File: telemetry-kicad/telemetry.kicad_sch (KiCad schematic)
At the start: 126 parts, among them J1 2601-1102, J2 RFPC-SMA27-F, J3 TC2030, J4 2601-1102, J5 MOLEX_104031-0811, J6 2601-1102, J7 USB_C_Receptacle_USB2.0_16P, Q1 DMP3099LQ-7, Q2 MMBT3904, SW1 CJS-1200TB1, SW2 CJS-1200TB1, SW3 SW_NRST, SW4 SW_BOOT0, U1 LMR33610ADDAR, U10 LC29HBAMD, U11 USBLC6-2SC6, U12 TXS0108EPW, U2 TPS2121RUXR, U3 ASM330LHHXG1TR, U4 TCAN337, U5 LM2940CT-5.0/LF01, U6 STM32H523RCT7, U7 TCAN337, U8 TLC59108IPWR, U9 TLC59108IPWR, Y1 ABM8AIG-24.000MHz-8-2Z-T

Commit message: ERC errors cleared
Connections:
- no-connect marks 15 -> 30
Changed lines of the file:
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@@
 	)
 	(no_connect
+		(at 100.33 176.53)
+	)
+	(no_connect
+		(at 100.33 179.07)
+	)
+	(no_connect
+		(at 100.33 181.61)
+	)
+	(no_connect
+		(at 39.37 186.69)
+	)
+	(no_connect
+		(at 39.37 189.23)
+	)
+	(no_connect
+		(at 39.37 191.77)
+	)
+	(no_connect
+		(at 39.37 217.17)
+	)
+	(no_connect
+		(at 39.37 219.71)
+	)
+	(no_connect
+		(at 39.37 181.61)
+	)
+	(no_connect
+		(at 353.06 172.72)
+	)
+	(no_connect
+		(at 353.06 175.26)
+	)
+	(no_connect
+		(at 353.06 177.8)
+	)
+	(no_connect
+		(at 410.21 172.72)
+	)
+	(no_connect
+		(at 410.21 175.26)
+	)
+	(no_connect
+		(at 410.21 177.8)
+	)
+	(no_connect
 		(at 171.45 217.17)
 	)
@@
 					(unit 1)
 				)
+			)
+		)
+	)
+	(symbol
+		(lib_id "power:PWR_FLAG")
+		(at 393.7 27.94 0)
+		(unit 1)
+		(body_style 1)
+		(exclude_from_sim no)
+		(in_bom yes)
+		(on_board yes)
+		(in_pos_files yes)
+		(dnp no)
+		(property "Reference" "#FLG01"
+			(at 393.7 29.845000000000002 0)
+			(hide yes)
+			(show_name no)
+			(do_not_autoplace no)
+			(effects
+				(font
+					(size 1.27 1.27)
+				)
+			)
+		)
+		(property "Value" "PWR_FLAG"
+			(at 393.7 31.75 0)
+			(show_name no)
+			(do_not_autoplace no)
+			(effects
+				(font
+					(size 1.27 1.27)
+				)
+			)
+		)
+		(property "Footprint" ""
+			(at 393.7 27.94 0)
+			(hide yes)
+			(show_name no)
+			(do_not_autoplace no)
+			(effects
+				(font
+					(size 1.27 1.27)
+				)
+			)
+		)
+		(property "Datasheet" ""
+			(at 393.7 27.94 0)
+			(hide yes)
+			(show_name no)
+			(do_not_autoplace no)
+			(effects
+				(font
+					(size 1.27 1.27)
+				)
+			)
+		)
+		(pin "1"
+		)
+		(instances
+			(project "telemetry"
+				(path "/3df6834d-aaf5-42e5-8a41-0f444a5b1186"
+					(reference "#FLG01")
+					(unit 1)
+				)
+			)
+		)
+	)
+	(symbol
+		(lib_id "power:PWR_FLAG")
+		(at 22.86 29.21 0)
+		(unit 1)
+		(body_style 1)
+		(exclude_from_sim no)
+		(in_bom yes)
+		(on_board yes)
+		(in_pos_files yes)
+		(dnp no)
+		(property "Reference" "#FLG02"
+			(at 22.86 31.115000000000002 0)
+			(hide yes)
+			(show_name no)
+			(do_not_autoplace no)
+			(effects
+				(font
+					(size 1.27 1.27)
+				)
+			)
+		)
+		(property "Value" "PWR_FLAG"
+			(at 22.86 33.02 0)
+			(show_name no)
+			(do_not_autoplace no)
+			(effects
+				(font
+					(size 1.27 1.27)
+				)
+			)
+		)
+		(property "Footprint" ""
+			(at 22.86 29.21 0)
+			(hide yes)
+			(show_name no)
+			(do_not_autoplace no)
+			(effects
+				(font
+					(size 1.27 1.27)
+				)
+			)
+		)
+		(property "Datasheet" ""
+			(at 22.86 29.21 0)
+			(hide yes)
+			(show_name no)
+			(do_not_autoplace no)
+			(effects
+				(font
+					(size 1.27 1.27)
+				)
+			)
+		)
+		(pin "1"
+		)
+		(instances
+			(project "telemetry"
+				(path "/3df6834d-aaf5-42e5-8a41-0f444a5b1186"
+					(reference "#FLG02")
+					(unit 1)
+				)
+			)
+		)
+	)
+	(symbol
+		(lib_id "power:PWR_FLAG")
+		(at 254.0 33.02 0)
+		(unit 1)
+		(body_style 1)
+		(exclude_from_sim no)
+		(in_bom yes)
+		(on_board yes)
+		(in_pos_files yes)
+		(dnp no)
+		(property "Reference" "#FLG03"
+			(at 254.0 34.925000000000004 0)
+			(hide yes)
+			(show_name no)
+			(do_not_autoplace no)
+			(effects
+				(font
+					(size 1.27 1.27)
+				)
+			)
+		)
+		(property "Value" "PWR_FLAG"
+			(at 254.0 36.830000000000005 0)
+			(show_name no)
+			(do_not_autoplace no)
+			(effects
+				(font
+					(size 1.27 1.27)
+				)
+			)
+		)
+		(property "Footprint" ""
+			(at 254.0 33.02 0)
+			(hide yes)
+			(show_name no)
+			(do_not_autoplace no)
+			(effects
+				(font
+					(size 1.27 1.27)
+				)
+			)
+		)
+		(property "Datasheet" ""
+			(at 254.0 33.02 0)
+			(hide yes)
+			(show_name no)
+			(do_not_autoplace no)
+			(effects
+				(font
+					(size 1.27 1.27)
+				)
+			)
+		)
+		(pin "1"
+		)
+		(instances
+			(project "telemetry"
+				(path "/3df6834d-aaf5-42e5-8a41-0f444a5b1186"
+					(reference "#FLG03")
+					(unit 1)
+				)

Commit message: Readme update
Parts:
- D2: footprint Capacitor_SMD:C_0402_1005Metric_Pad0.74x0.62mm_HandSolder -> telemetry:D20V0L1B2LP-7B
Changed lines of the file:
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@@
 			)
 		)
-		(property "Footprint" "Capacitor_SMD:C_0402_1005Metric_Pad0.74x0.62mm_HandSolder"
+		(property "Footprint" "telemetry:D20V0L1B2LP-7B"
 			(at 35.56 43.18 0)
 			(hide yes)

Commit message: Changed to LC29HEAMD for better RTK 10cm -> 1cm. Changed to active antenna, some passives required.
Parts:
- removed D2: D20V0L1B2LP-7B, telemetry:D20V0L1B2LP-7B, symbol Device:D_TVS
- removed U10: LC29HBAMD, telemetry:LC29HBAMD, symbol telemetry:LC29HBAMD
- removed U12: TXS0108EPW, Package_SO:TSSOP-20_4.4x6.5mm_P0.65mm, symbol Logic_LevelTranslator:TXS0108EPW
- added C39: 100nF, Capacitor_SMD:C_0402_1005Metric_Pad0.74x0.62mm_HandSolder, symbol Device:C
- added C40: 100pF, Capacitor_SMD:C_0402_1005Metric_Pad0.74x0.62mm_HandSolder, symbol Device:C
- added D2: PESD0402-140, telemetry:PESD0402-140, symbol telemetry:PESD0402-140
- added L2: LQW15AN56NG00D, telemetry:LQW15AN56NG00D, symbol telemetry:LQW15AN56NG00D
- added R40: 10, Resistor_SMD:R_0402_1005Metric_Pad0.72x0.64mm_HandSolder, symbol Device:R_US
- added U13: LC29HEAMD, telemetry:LC29HEAMD, symbol telemetry:LC29HEAMD
- added U14: TXS0104EPW, Package_SO:TSSOP-14_4.4x5mm_P0.65mm, symbol Logic_LevelTranslator:TXS0104EPW
- C36: value 1uF -> 100nF
- C38: value 100nF -> 100pF
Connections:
- net +3.3V: now also C39.2, U13.22 (V_BCKP), U13.23 (VCC), U14.14 (V_{CCB}); no longer C36.1, C38.2
- net ANT: now also C40.1, D2.2 (A2), L2.1
- net DSEL_1: now also U13.5 (D_SEL1)
- net DSEL_2: now also R38.2, U13.6 (D_SEL2); no longer R38.1
- net GND: now also C38.2, C39.1, D2.1 (A1), U13.10 (GND), U13.12 (GND), U13.13 (GND), U13.24 (GND), U14.7 (GND); no longer C38.1, R38.2
- net GNSS_RESET_N: now also U13.8 (RESET_N)
- net TIMERIN_GNSS: now also U14.10 (B4)
- net TIMERIN_GNSS_2V8: now also U13.3 (1PPS), U14.5 (A4)
- net VDD_EXT: now also R38.1, U13.7 (VDD_EXT), U14.1 (V_{CCA}), U14.8 (OE)
- net CLK_GNSS: no longer names the net of U6.16 (PA2)
- net CS_GNSS: no longer names the net of U6.17 (PA3)
- net MISO_GNSS renamed TXD1_GNSS
- net TXD1_GNSS: now also U14.11 (B3)
- net MOSI_GNSS renamed RXD1_GNSS
- net RXD1_GNSS: now also U14.12 (B2)
- new net: C36.1, C38.1, L2.2, R40.1
- new net ANT_ON: U13.14 (ANT_ON)
- new net RF_IN: C40.2, U13.11 (RF_IN)
- new net RXD1_GNSS_2V8: U13.21 (RXD1/SPI_MOSI), U14.3 (A2)
- new net TXD1_GNSS_2V8: U13.20 (TXD1/SPI_MISO), U14.4 (A3)
- new net VDD_RF: R40.2, U13.9 (VDD_RF)
- no-connect marks 30 -> 29
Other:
- moved on the sheet: C23, C24, Q2, R35, R36, R37, R38, R39, TP4

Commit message: Added two GNSS modules for heading information
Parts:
- added C41, C42: 100pF, Capacitor_SMD:C_0402_1005Metric_Pad0.74x0.62mm_HandSolder, symbol Device:C
- added C43, C47: 100nF, Capacitor_SMD:C_0402_1005Metric_Pad0.74x0.62mm_HandSolder, symbol Device:C
- added C46: 10uF, Capacitor_SMD:C_0402_1005Metric_Pad0.74x0.62mm_HandSolder, symbol Device:C
- added C48: 1uF, Capacitor_SMD:C_0402_1005Metric_Pad0.74x0.62mm_HandSolder, symbol Device:C
- added D5: PESD0402-140, telemetry:PESD0402-140, symbol telemetry:PESD0402-140
- added J8: RFPC-SMA27-F, telemetry:RFPC-SMA27-F, symbol telemetry:RFPC-SMA27-F
- added L3: LQW15AN56NG00D, telemetry:LQW15AN56NG00D, symbol telemetry:LQW15AN56NG00D
- added R41: 10, Resistor_SMD:R_0402_1005Metric_Pad0.72x0.64mm_HandSolder, symbol Device:R_US
- added R42, R43: 39k, Resistor_SMD:R_0402_1005Metric_Pad0.72x0.64mm_HandSolder, symbol Device:R_US
- added U15: LC29HEAMD, telemetry:LC29HEAMD, symbol telemetry:LC29HEAMD
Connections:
- net +3.3V: now also C46.2, C47.2, C48.1, U15.22 (V_BCKP), U15.23 (VCC)
- net GND: now also C41.2, C43.2, C46.1, C47.1, C48.2, D5.1 (A1), J8.G1, J8.G2, J8.G3, J8.G4, U15.10 (GND), U15.12 (GND), U15.13 (GND), U15.24 (GND)
- net GNSS_RESET_N: now also U15.8 (RESET_N)
- net RXD2_GNSS_2V8_2: now reaches U13.15 (TXD2)
- net RXD2_GNSS_2V8_2: now also U15.16 (RXD2)
- net TXD2_GNSS_2V8_2: now reaches U13.16 (RXD2)
- net TXD2_GNSS_2V8_2: now also U15.15 (TXD2)
- net ANT renamed ANT1
- net ANT_ON renamed ANT_ON_1
- net DSEL_1 renamed DSEL_1_1
- net DSEL_2 renamed DSEL_2_1
- net RF_IN renamed RF_IN_1
- net RXD1_GNSS_2V8 renamed RXD1_GNSS_2V8_1
- net TIMERIN_GNSS_2V8 renamed TIMERIN_GNSS_2V8_1
- net TXD1_GNSS_2V8 renamed TXD1_GNSS_2V8_1
- net VDD_EXT renamed VDD_EXT_1
- net VDD_RF renamed VDD_RF_1
- new net: C41.1, C43.1, L3.2, R41.1
- new net ANT2: C42.1, D5.2 (A2), J8.1, L3.1
- new net ANT_ON_2: U15.14 (ANT_ON)
- new net DSEL_1_2: R43.2, U15.5 (D_SEL1)
- new net DSEL_2_2: R42.2, U15.6 (D_SEL2)
- new net RF_IN_2: C42.2, U15.11 (RF_IN)
- new net VDD_EXT_2: R42.1, R43.1, U15.7 (VDD_EXT)
- new net VDD_RF_2: R41.2, U15.9 (VDD_RF)
- no-connect marks 29 -> 36
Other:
- note added: "GNSS Base Antenna Connector"
- note added: "GNSS Base Module"
- note added: "GNSS Rover Antenna Connector"
- note added: "GNSS Rover Decoupling"
- note added: "GNSS Rover Module"
- note removed: "GNSS Antenna Connector"
- note removed: "GNSS Decoupling"
- note removed: "GNSS Module"
- moved on the sheet: J2, J3, Q2, R36, R37

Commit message: Switched to TC2030 with legs, small fixes. 3D models and LDO changed.
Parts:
- J3: footprint Connector:Tag-Connect_TC2030-IDC-NL_2x03_P1.27mm_Vertical -> Connector:Tag-Connect_TC2030-IDC-FP_2x03_P1.27mm_Vertical
- U5: footprint telemetry:LM2940CT-5.0-LF01 -> Package_TO_SOT_SMD:TO-263-3_TabPin2
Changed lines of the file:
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@@
 			)
 		)
-		(property "Footprint" "telemetry:LM2940CT-5.0-LF01"
+		(property "Footprint" "Package_TO_SOT_SMD:TO-263-3_TabPin2"
 			(at 412.75 113.03 0)
 			(hide yes)
@@
 			)
 		)
-		(property "Footprint" "Connector:Tag-Connect_TC2030-IDC-NL_2x03_P1.27mm_Vertical"
+		(property "Footprint" "Connector:Tag-Connect_TC2030-IDC-FP_2x03_P1.27mm_Vertical"
 			(at 129.54 81.28 0)
 			(hide yes)

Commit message: Changed decoupling from 1uF to 100nF, added capcitance to Power Mux output
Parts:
- added C5, C6: 22uF, Capacitor_SMD:C_0402_1005Metric_Pad0.74x0.62mm_HandSolder, symbol Device:C
- C30: renamed from C25; value 1uF -> 100nF
- C31: renamed from C26; value 1uF -> 100nF
- C32: renamed from C27; value 1uF -> 100nF
- C33: renamed from C28; value 1uF -> 100nF
- C34: renamed from C29; value 1uF -> 100nF
- C35: renamed from C30; value 1uF -> 100nF
- renumbered C8 to C10, C9 to C11, C10 to C12, C11 to C13, C12 to C14, C13 to C15, C14 to C16, C15 to C17, C16 to C18, C17 to C19, C18 to C20, C19 to C21, C20 to C22, C21 to C23, C22 to C24, C23 to C25, C24 to C26, C40 to C27, C38 to C28, C36 to C29, C4 to C3, C31 to C36, C32 to C37, C33 to C38, C34 to C39, C3 to C4, C35 to C40, C39 to C41, C37 to C42, C46 to C43, C47 to C44, C48 to C45, C42 to C46, C41 to C47, C43 to C48, C5 to C7, C6 to C8, C7 to C9, D3 to D2, D4 to D3, D2 to D4, J3 to J2, J5 to J3, J6 to J5, J7 to J6, J2 to J7, R40 to R38, R38 to R39, R39 to R40, U13 to U10, U14 to U12, U15 to U13
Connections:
- net GND: now also C5.2, C6.2
- net V_IN: now also C5.1, C6.1
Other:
- moved on the sheet: C1, C10, C11, C12, C3, C31, C4, C7, C8, C9, D2, J1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

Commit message: Impediance measurment added, full pi filter for each antenna implimented
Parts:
- added C28, C29, C49, C50: 0, Capacitor_SMD:C_0402_1005Metric_Pad0.74x0.62mm_HandSolder, symbol Device:C
- added J10, J9: RFPC-SMA27-F, telemetry:RFPC-SMA27-F, symbol telemetry:RFPC-SMA27-F
- added R35, R42: 0, Resistor_SMD:R_0402_1005Metric_Pad0.72x0.64mm_HandSolder, symbol Device:R_US
- renumbered C28 to C30, C29 to C31, C30 to C32, C31 to C33, C32 to C34, C33 to C35, C34 to C36, C35 to C37, C36 to C38, C37 to C39, C38 to C40, C39 to C41, C40 to C42, C41 to C43, C42 to C44, C43 to C45, C44 to C46, C45 to C47, C46 to C48, C47 to C51, C48 to C52, R35 to R36, R36 to R37, R37 to R38, R38 to R39, R39 to R40, R40 to R41, R41 to R43, R42 to R44, R43 to R45
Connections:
- net GND: now also C28.2, C29.2, C49.2, C50.2, J10.G1, J10.G2, J10.G3, J10.G4, J9.G1, J9.G2, J9.G3, J9.G4
- net RF_IN_1: now also C29.1, R35.2; no longer C27.2
- net RF_IN_2: now also C50.1, R42.2; no longer C48.2
- new net: C27.2, C28.1, R35.1
- new net: C48.2, C49.1, R42.1
- new net ANT3: J10.1, J9.1

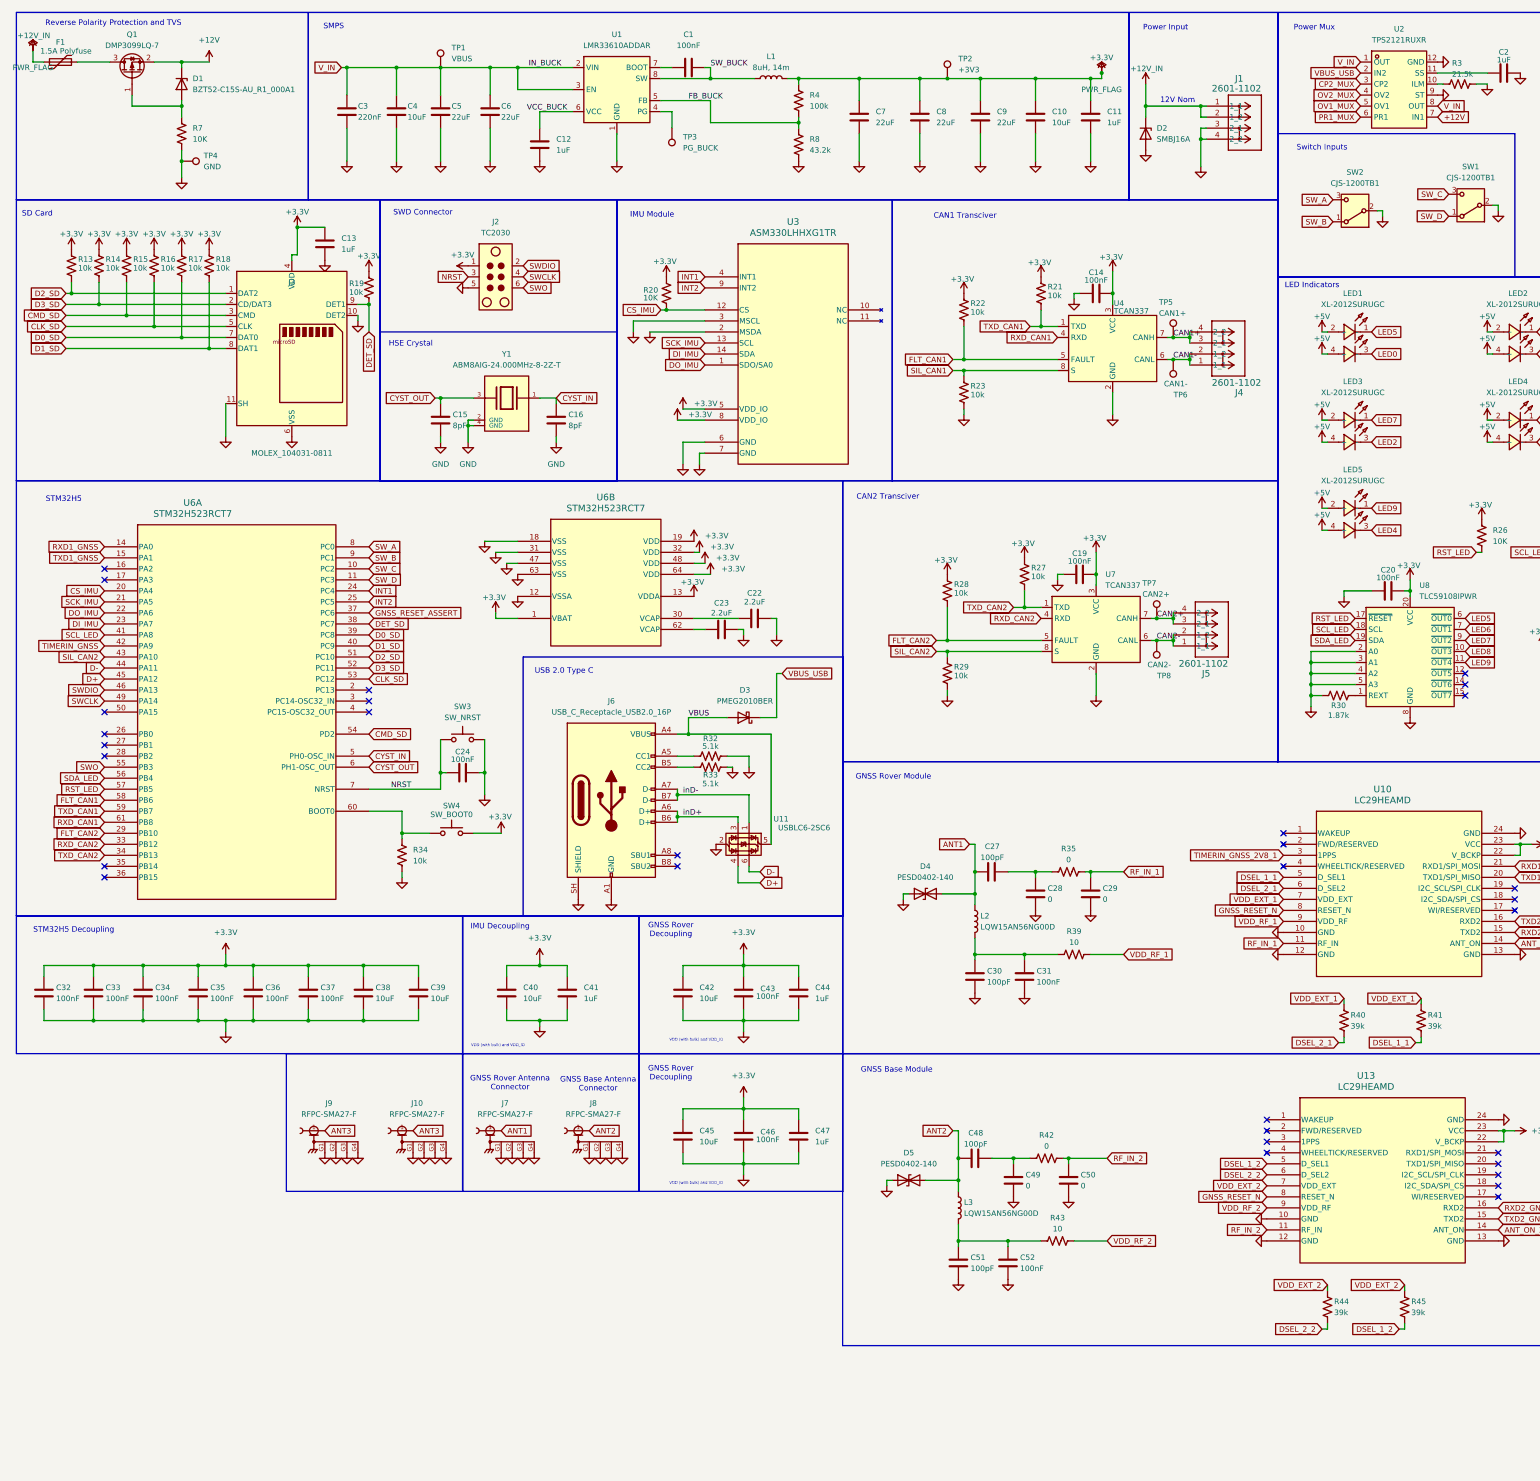
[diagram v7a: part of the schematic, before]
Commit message: need to route the second sd card module
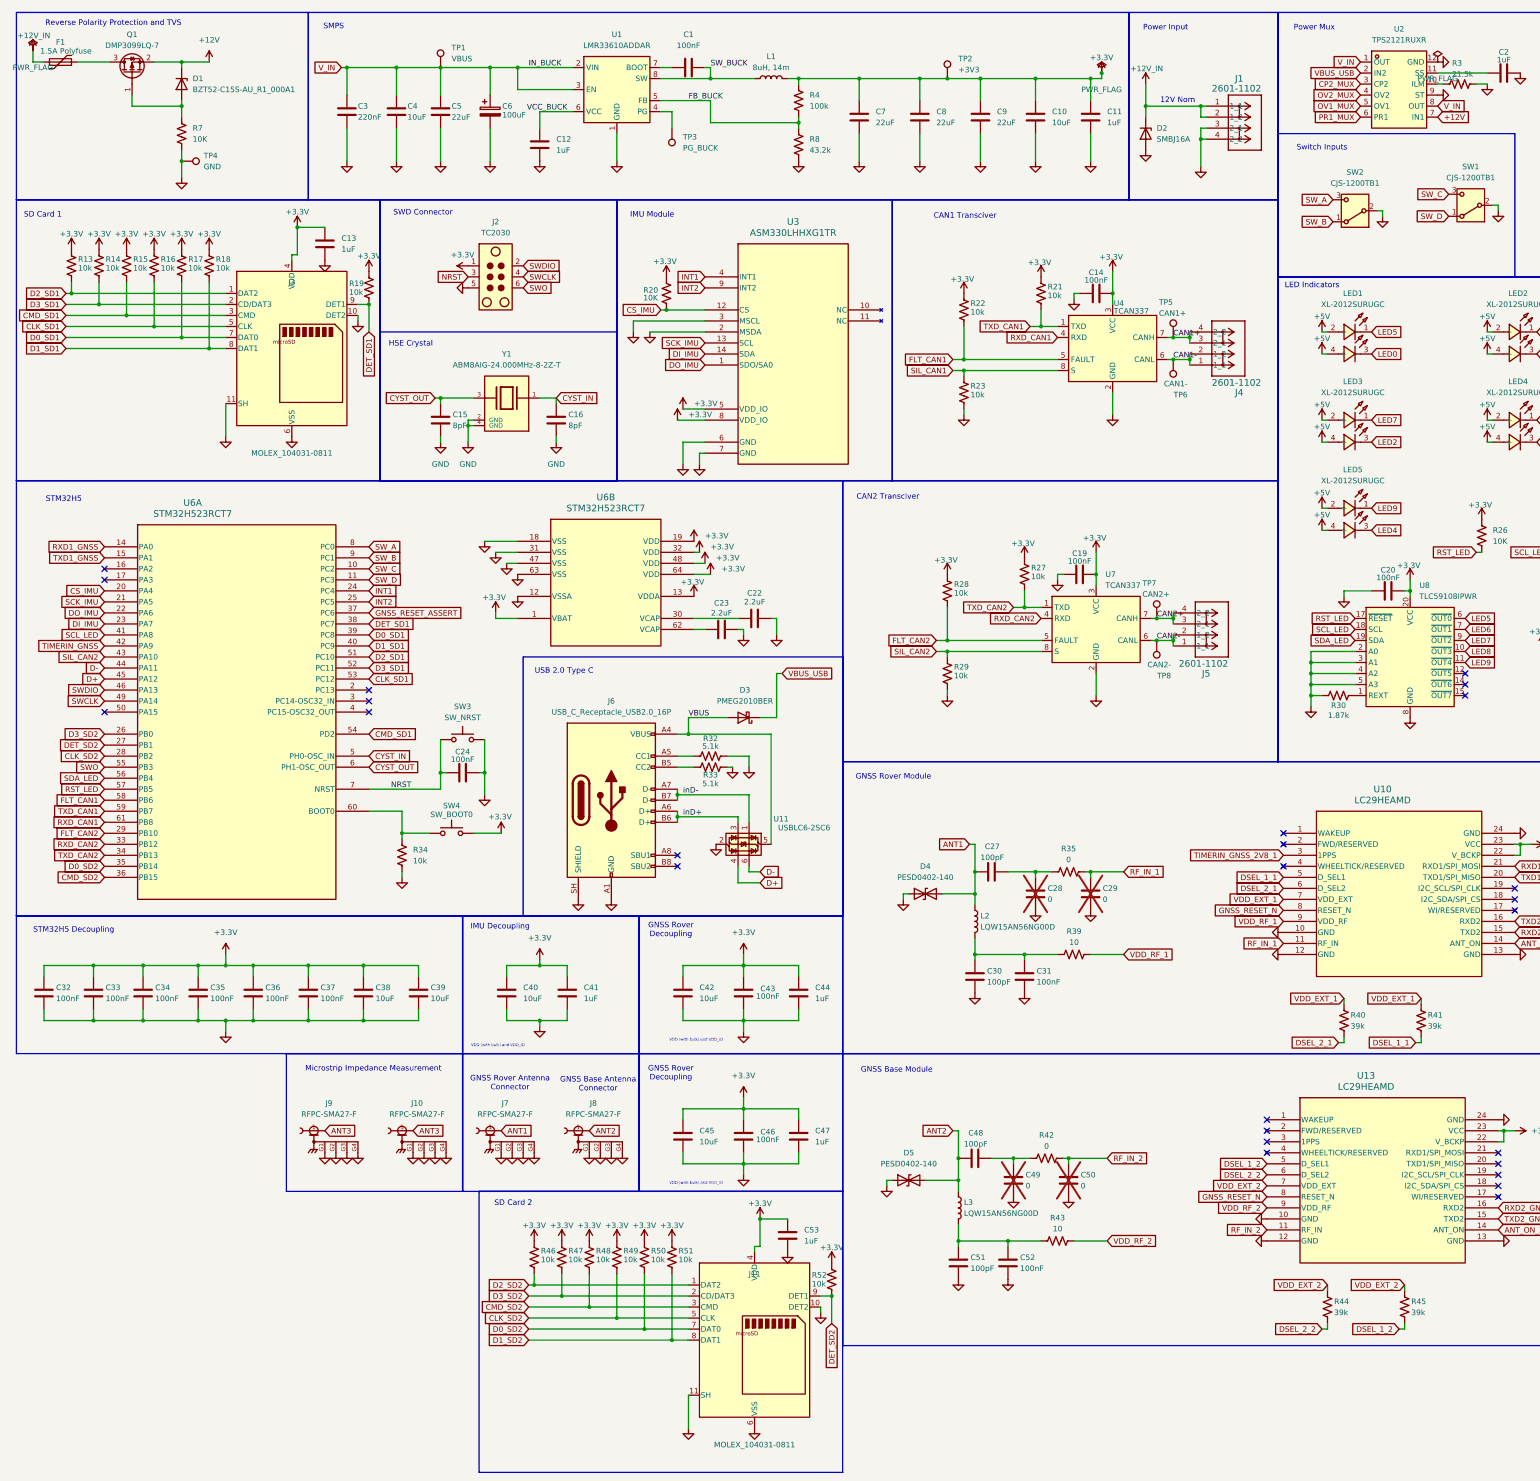
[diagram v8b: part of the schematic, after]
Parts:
- removed C6: 22uF, Capacitor_SMD:C_0402_1005Metric_Pad0.74x0.62mm_HandSolder, symbol Device:C
- added C53: 1uF, Capacitor_SMD:C_0402_1005Metric_Pad0.74x0.62mm_HandSolder, symbol Device:C
- added C6: 100uF, Capacitor_SMD:CP_Elec_6.3x7.7, symbol Device:C_Polarized
- added J11: MOLEX_104031-0811, telemetry:MOLEX_104031-0811, symbol telemetry:MOLEX_104031-0811
- added R46, R47, R48, R49, R50, R51, R52: 10k, Resistor_SMD:R_0402_1005Metric_Pad0.72x0.64mm_HandSolder, symbol Device:R_US
- C28, C29, C49, C50: now not fitted
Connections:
- net +3.3V: now also C53.1, J11.4 (VDD), R46.1, R47.1, R48.1, R49.1, R50.1, R51.1, R52.1
- net GND: now also C53.2, C6.2, J11.10 (DET2), J11.11 (SH), J11.6 (VSS)
- net V_IN: now also C6.1
- net D3_SD2: now reaches U6.26 (PB0)
- net D3_SD2: now also J11.2 (CD/DAT3), R47.2
- net DET_SD2: now reaches U6.27 (PB1)
- net DET_SD2: now also J11.9 (DET1), R52.2
- net CLK_SD2: now reaches U6.28 (PB2)
- net CLK_SD2: now also J11.5 (CLK), R49.2
- net D0_SD2: now reaches U6.35 (PB14)
- net D0_SD2: now also J11.7 (DAT0), R50.2
- net CMD_SD2: now reaches U6.36 (PB15)
- net CMD_SD2: now also J11.3 (CMD), R48.2
- net CLK_SD renamed CLK_SD1
- net CMD_SD renamed CMD_SD1
- net D0_SD renamed D0_SD1
- net D1_SD renamed D1_SD1
- net D2_SD renamed D2_SD1
- net D3_SD renamed D3_SD1
- net DET_SD renamed DET_SD1
- new net D1_SD2: J11.8 (DAT1), R51.2
- new net D2_SD2: J11.1 (DAT2), R46.2
- no-connect marks 36 -> 31
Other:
- note added: "Microstrip Impedance Measurement"
- note added: "SD Card 1"
- note added: "SD Card 2"
- note removed: "SD Card"
